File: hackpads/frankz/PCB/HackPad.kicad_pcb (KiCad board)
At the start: 2 copper layers, 63 x 82 mm, 29 parts, among them SW1 SW_Push_45deg, SW10 SW_Push_45deg, SW11 RotaryEncoder_Switch, SW12 RotaryEncoder_Switch, SW2 SW_Push_45deg, SW3 SW_Push_45deg, SW4 SW_Push_45deg, SW5 SW_Push_45deg, SW6 SW_Push_45deg, SW7 SW_Push_45deg, SW8 SW_Push_45deg, SW9 SW_Push_45deg, U2 MOUDLE-SEEEDUINO-XIAO

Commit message: Update PCB
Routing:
- net 1pinA: track 25.8 -> 24.6 mm
- net 1pinB: track 45.4 -> 44.6 mm
- net 2pinS2: track 110.3 -> 109.4 mm
- net 2pinB: track 70.9 -> 70.1 mm
- net 2pinA: track 59.5 -> 58.9 mm
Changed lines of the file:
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@@
 		(tags "Diode DO-35_SOD27 series Axial Horizontal pin pitch 7.62mm  length 4mm diameter 2mm")
 		(property "Reference" "D11"
-			(at 3.81 2.12 360)
+			(at 3.81 2.12 0)
 			(layer "B.SilkS")
 			(hide yes)
@@
 		)
 		(property "Value" "D"
-			(at 3.81 -2.12 360)
+			(at 3.81 -2.12 0)
 			(layer "B.Fab")
 			(hide yes)
@@
 		(tags "Diode DO-35_SOD27 series Axial Horizontal pin pitch 7.62mm  length 4mm diameter 2mm")
 		(property "Reference" "D10"
-			(at 3.81 2.12 360)
+			(at 3.81 2.12 0)
 			(layer "B.SilkS")
 			(hide yes)
@@
 		)
 		(property "Value" "D"
-			(at 3.81 -2.12 360)
+			(at 3.81 -2.12 0)
 			(layer "B.Fab")
 			(hide yes)
@@
 	)
 	(segment
-		(start 68.5 51.25)
-		(end 68.5 41.25)
-		(width 0.2)
-		(layer "B.Cu")
-		(net 19)
-	)
-	(segment
-		(start 67.440001 58.960001)
-		(end 67.440001 52.309999)
-		(width 0.2)
-		(layer "B.Cu")
-		(net 19)
-	)
-	(segment
 		(start 68.69 79.21)
 		(end 68.69 89.694365)
@@
 	)
 	(segment
+		(start 69 41.25)
+		(end 79.5 41.25)
+		(width 0.2)
+		(layer "B.Cu")
+		(net 19)
+	)
+	(segment
 		(start 61.565 36.55)
 		(end 63.8 36.55)
@@
 	)
 	(segment
-		(start 68.69 60.21)
+		(start 67.5 78.02)
+		(end 68.69 79.21)
+		(width 0.2)
+		(layer "B.Cu")
+		(net 19)
+	)
+	(segment
+		(start 67.440001 52.309999)
 		(end 67.440001 58.960001)
 		(width 0.2)
@@
 	)
 	(segment
-		(start 63.8 36.55)
-		(end 68.5 41.25)
+		(start 67.440001 58.960001)
+		(end 68.69 60.21)
 		(width 0.2)
 		(layer "B.Cu")
@@
 	)
 	(segment
-		(start 67.5 78.02)
-		(end 68.69 79.21)
+		(start 67.5 71.884365)
+		(end 67.5 78.02)
 		(width 0.2)
 		(layer "B.Cu")
@@
 	)
 	(segment
-		(start 68.5 41.25)
-		(end 79.5 41.25)
+		(start 68.69 70.694365)
+		(end 67.5 71.884365)
 		(width 0.2)
 		(layer "B.Cu")
@@
 	)
 	(segment
-		(start 67.440001 52.309999)
+		(start 68.5 41.25)
 		(end 68.5 51.25)
 		(width 0.2)
@@
 	)
 	(segment
-		(start 67.5 71.884365)
-		(end 67.5 78.02)
+		(start 67.59 90.794365)
+		(end 67.59 97.11)
 		(width 0.2)
 		(layer "B.Cu")
@@
 	)
 	(segment
-		(start 68.69 70.694365)
-		(end 67.5 71.884365)
+		(start 68.5 51.25)
+		(end 67.440001 52.309999)
 		(width 0.2)
 		(layer "B.Cu")
@@
 	)
 	(segment
-		(start 67.59 90.794365)
-		(end 67.59 97.11)
+		(start 68.5 41.75)
+		(end 69 41.25)
+		(width 0.2)
+		(layer "B.Cu")
+		(net 19)
+	)
+	(segment
+		(start 63.8 36.55)
+		(end 68.5 41.25)
 		(width 0.2)
 		(layer "B.Cu")
@@
 	)
 	(segment
+		(start 99 55.25)
+		(end 100.5 53.75)
+		(width 0.2)
+		(layer "B.Cu")
+		(net 20)
+	)
+	(segment
 		(start 100.5 43.25)
 		(end 98.5 41.25)
@@
 	)
 	(segment
-		(start 100.5 55.25)
+		(start 100.5 53.75)
 		(end 100.5 43.25)
 		(width 0.2)
@@
 	)
 	(segment
-		(start 91.5 55.25)
-		(end 100.5 55.25)
+		(start 87.69 79.21)
+		(end 87.69 89.694365)
 		(width 0.2)
 		(layer "B.Cu")
@@
 	)
 	(segment
-		(start 87.69 79.21)
-		(end 87.69 89.694365)
+		(start 87.645 70.739365)
+		(end 86.59 71.794365)
 		(width 0.2)
 		(layer "B.Cu")
@@
 	)
 	(segment
-		(start 87.645 70.739365)
-		(end 86.59 71.794365)
+		(start 87.69 59.06)
+		(end 91.5 55.25)
 		(width 0.2)
 		(layer "B.Cu")
@@
 	)
 	(segment
-		(start 86.59 97.11)
-		(end 87.69 98.21)
+		(start 91.5 55.25)
+		(end 99 55.25)
 		(width 0.2)
 		(layer "B.Cu")
@@
 	)
 	(segment
-		(start 87.69 59.06)
-		(end 91.5 55.25)
+		(start 86.59 97.11)
+		(end 87.69 98.21)
 		(width 0.2)
 		(layer "B.Cu")
@@
 	)
 	(segment
-		(start 59 40.25)
+		(start 51.26 36.25)
+		(end 58 36.25)
+		(width 0.2)
+		(layer "F.Cu")
+		(net 23)
+	)
+	(segment
+		(start 60 40.25)
 		(end 64 40.25)
 		(width 0.2)
@@
 	)
 	(segment
+		(start 45.88 41.63)
+		(end 51.26 36.25)
+		(width 0.2)
+		(layer "F.Cu")
+		(net 23)
+	)
+	(segment
+		(start 59 39.25)
+		(end 60 40.25)
+		(width 0.2)
+		(layer "F.Cu")
+		(net 23)
+	)
+	(segment
 		(start 64 40.25)
 		(end 65 41.25)
@@
 	)
 	(segment
-		(start 51.26 36.25)
-		(end 59 36.25)
+		(start 58 36.25)
+		(end 59 37.25)
 		(width 0.2)
 		(layer "F.Cu")
@@
 	)
 	(segment
-		(start 45.88 41.63)
-		(end 51.26 36.25)
+		(start 59 37.25)
+		(end 59 39.25)
 		(width 0.2)
 		(layer "F.Cu")
@@
 	)
 	(segment
-		(start 59 36.25)
-		(end 59 40.25)
+		(start 45.88 44.17)
+		(end 48 46.29)
 		(width 0.2)
 		(layer "F.Cu")
-		(net 23)
+		(net 24)
 	)
 	(segment
 		(start 48 46.29)
-		(end 48 54.75)
+		(end 48 53.75)
 		(width 0.2)
 		(layer "F.Cu")
@@
 	)
 	(segment
-		(start 45.88 44.17)
-		(end 48 46.29)
+		(start 48 53.75)
+		(end 49 54.75)
 		(width 0.2)
 		(layer "F.Cu")
@@
 	)
 	(segment
-		(start 71 54.75)
-		(end 71 52.25)
+		(start 49 54.75)
+		(end 70.5 54.75)
 		(width 0.2)
 		(layer "F.Cu")
@@
 	)
 	(segment
-		(start 48 54.75)
-		(end 71 54.75)
+		(start 70.5 54.75)
+		(end 71 54.25)
 		(width 0.2)
 		(layer "F.Cu")
@@
 	)
 	(segment
+		(start 71 54.25)
+		(end 71 52.25)
+		(width 0.2)
+		(layer "F.Cu")
+		(net 24)
+	)
+	(segment
+		(start 85.3 39.95)
+		(end 77.2 31.85)
+		(width 0.2)
+		(layer "B.Cu")
+		(net 25)
+	)
+	(segment
 		(start 85.3 44.95)
 		(end 85.3 39.95)
@@
 	)
 	(segment
-		(start 43 46.85)
-		(end 45.4 49.25)
+		(start 44.334314 31.85)
+		(end 43 33.184314)
+		(width 0.2)
+		(layer "B.Cu")
+		(net 25)
+	)
+	(segment
+		(start 77.2 31.85)
+		(end 44.334314 31.85)
 		(width 0.2)
 		(layer "B.Cu")
@@
 	)
 	(segment
-		(start 43 31.85)
+		(start 43 33.184314)
 		(end 43 46.85)
 		(width 0.2)
@@
 	)
 	(segment
-		(start 85.3 39.95)
-		(end 77.2 31.85)
+		(start 43 46.85)
+		(end 45.4 49.25)
 		(width 0.2)
 		(layer "B.Cu")
@@
 	)
 	(segment
-		(start 77.2 31.85)
-		(end 43 31.85)
+		(start 44.5 32.25)
+		(end 43.5 33.25)
 		(width 0.2)
 		(layer "B.Cu")
-		(net 25)
+		(net 26)
 	)
 	(segment
-		(start 84 41.25)
-		(end 75 32.25)
+		(start 43.5 33.25)
+		(end 43.5 44.81)
 		(width 0.2)
 		(layer "B.Cu")
@@
 	)
 	(segment
-		(start 75 32.25)
-		(end 43.5 32.25)
+		(start 43.5 44.81)
+		(end 45.4 46.71)
 		(width 0.2)
 		(layer "B.Cu")
@@
 	)
 	(segment
-		(start 43.5 32.25)
-		(end 43.5 44.81)
+		(start 84 41.25)
+		(end 75 32.25)
 		(width 0.2)
 		(layer "B.Cu")
@@
 	)
 	(segment
-		(start 43.5 44.81)
-		(end 45.4 46.71)
+		(start 75 32.25)
+		(end 44.5 32.25)
 		(width 0.2)
 		(layer "B.Cu")
@@
 		(polygon
 			(pts
-				(xy 33 25.25) (xy 117.5 25.25) (xy 117.5 128.75) (xy 28.5 128.25)
+				(xy 112 25.75) (xy 32 25.25) (xy 31.5 125.25) (xy 124 124.75)
 			)
 		)

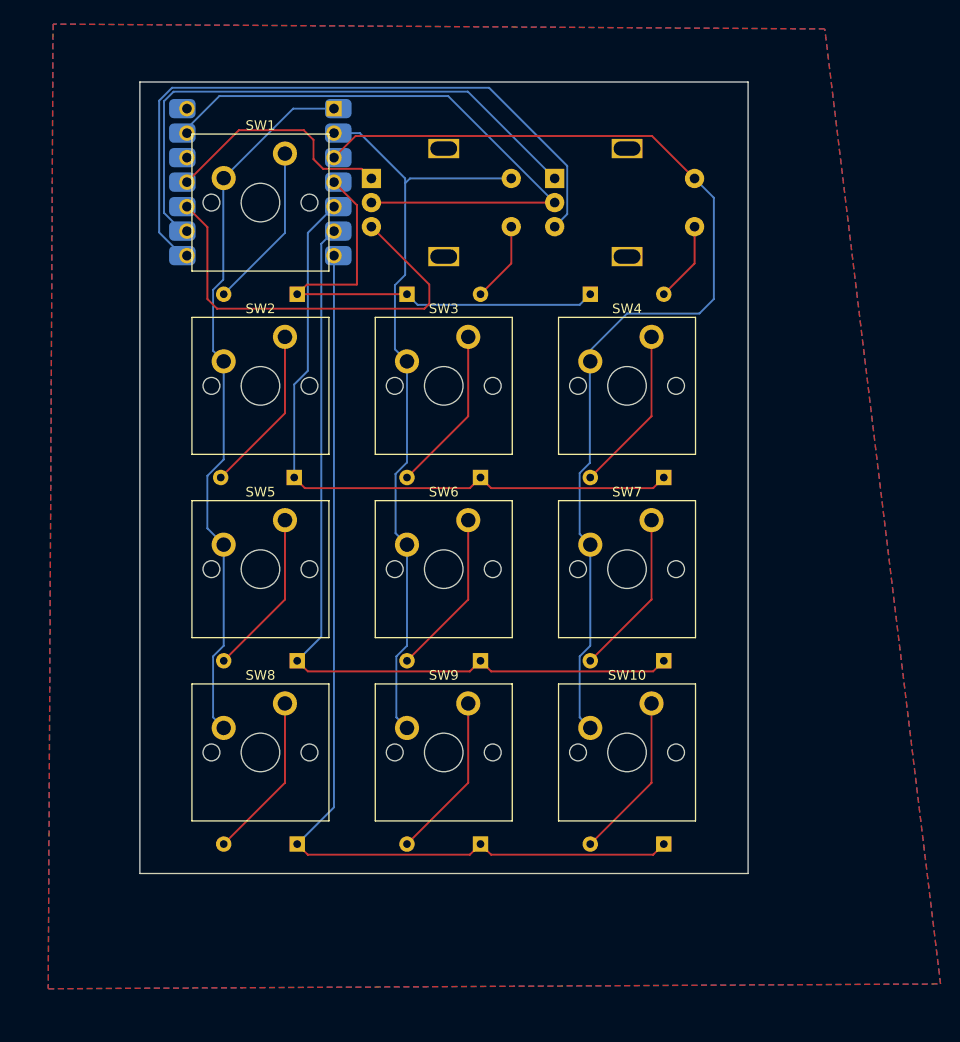
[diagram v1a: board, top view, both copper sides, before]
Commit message: Added production folder and reorganized
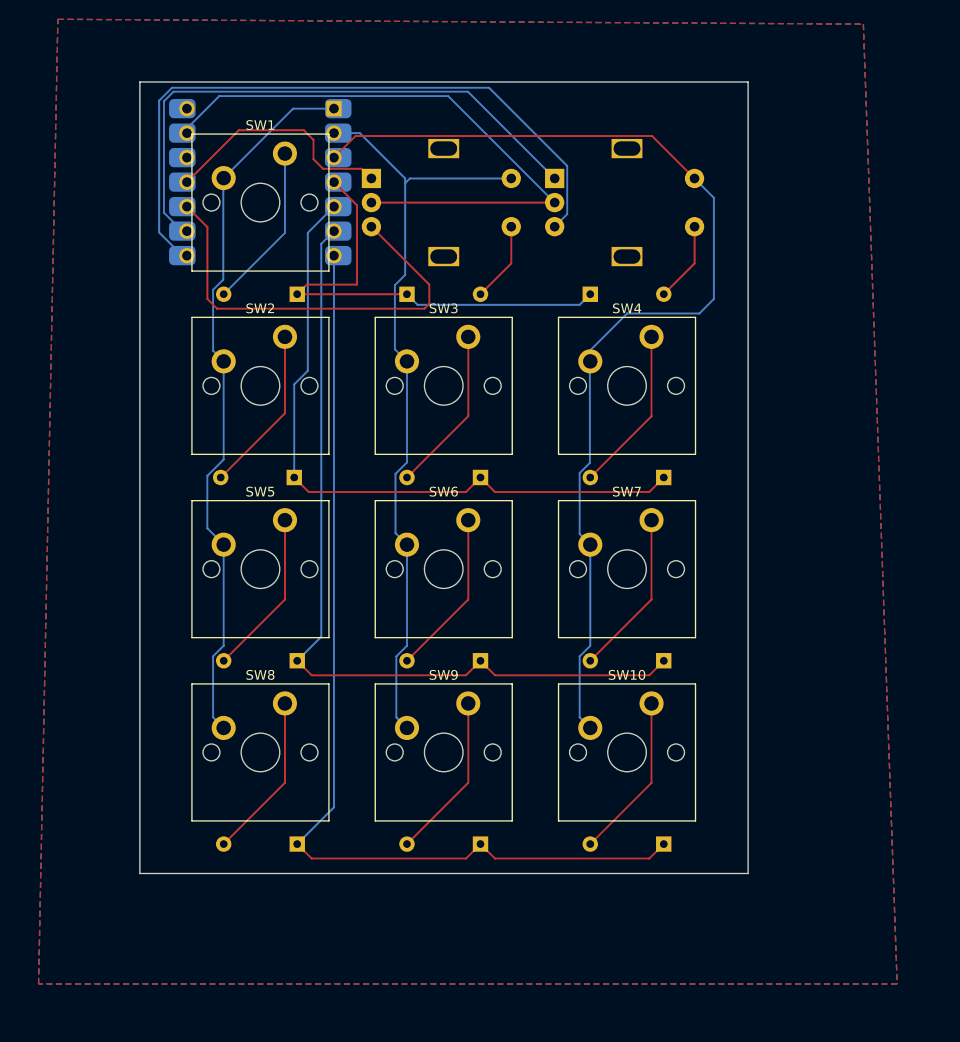
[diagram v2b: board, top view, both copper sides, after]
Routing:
- net ROW2: track 85.9 -> 86.6 mm
- net ROW3: track 102.4 -> 103.1 mm
- net ROW1: track 69.9 -> 70.6 mm
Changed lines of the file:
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@@
 			(usegerberattributes yes)
 			(usegerberadvancedattributes yes)
-			(creategerberjobfile yes)
+			(creategerberjobfile no)
 			(dashed_line_dash_ratio 12.000000)
 			(dashed_line_gap_ratio 3.000000)
@@
 			(psa4output no)
 			(plotreference yes)
-			(plotvalue yes)
+			(plotvalue no)
 			(plotfptext yes)
 			(plotinvisibletext no)
 			(sketchpadsonfab no)
-			(subtractmaskfromsilk no)
+			(subtractmaskfromsilk yes)
 			(outputformat 1)
 			(mirror no)
-			(drillshape 1)
+			(drillshape 0)
 			(scaleselection 1)
-			(outputdirectory "")
+			(outputdirectory "./")
 		)
 	)
@@
 	)
 	(segment
-		(start 58.1 73.35)
-		(end 75.21 73.35)
+		(start 77.81 73.75)
+		(end 93.81 73.75)
 		(width 0.2)
 		(layer "F.Cu")
@@
 	)
 	(segment
-		(start 94.21 73.35)
-		(end 95.31 72.25)
+		(start 74.81 73.75)
+		(end 76.31 72.25)
 		(width 0.2)
 		(layer "F.Cu")
@@
 	)
 	(segment
-		(start 75.21 73.35)
-		(end 76.31 72.25)
+		(start 93.81 73.75)
+		(end 95.31 72.25)
 		(width 0.2)
 		(layer "F.Cu")
@@
 	)
 	(segment
-		(start 77.41 73.35)
-		(end 94.21 73.35)
+		(start 76.31 72.25)
+		(end 77.81 73.75)
 		(width 0.2)
 		(layer "F.Cu")
@@
 	(segment
 		(start 57 72.25)
-		(end 58.1 73.35)
+		(end 58.5 73.75)
 		(width 0.2)
 		(layer "F.Cu")
@@
 	)
 	(segment
-		(start 76.31 72.25)
-		(end 77.41 73.35)
+		(start 58.5 73.75)
+		(end 74.81 73.75)
 		(width 0.2)
 		(layer "F.Cu")
@@
 	)
 	(segment
-		(start 75.21 92.35)
-		(end 76.31 91.25)
+		(start 58.81 92.75)
+		(end 74.81 92.75)
 		(width 0.2)
 		(layer "F.Cu")
@@
 	)
 	(segment
-		(start 57.31 91.25)
-		(end 58.41 92.35)
+		(start 74.81 92.75)
+		(end 76.31 91.25)
 		(width 0.2)
 		(layer "F.Cu")
@@
 	)
 	(segment
-		(start 76.31 91.25)
-		(end 77.41 92.35)
+		(start 77.81 92.75)
+		(end 93.81 92.75)
 		(width 0.2)
 		(layer "F.Cu")
@@
 	)
 	(segment
-		(start 58.41 92.35)
-		(end 75.21 92.35)
+		(start 93.81 92.75)
+		(end 95.31 91.25)
 		(width 0.2)
 		(layer "F.Cu")
@@
 	)
 	(segment
-		(start 94.21 92.35)
-		(end 95.31 91.25)
+		(start 76.31 91.25)
+		(end 77.81 92.75)
 		(width 0.2)
 		(layer "F.Cu")
@@
 	)
 	(segment
-		(start 77.41 92.35)
-		(end 94.21 92.35)
+		(start 57.31 91.25)
+		(end 58.81 92.75)
 		(width 0.2)
 		(layer "F.Cu")
@@
 	)
 	(segment
-		(start 77.41 111.35)
-		(end 94.21 111.35)
+		(start 76.31 110.25)
+		(end 77.81 111.75)
 		(width 0.2)
 		(layer "F.Cu")
@@
 	)
 	(segment
-		(start 76.31 110.25)
-		(end 77.41 111.35)
+		(start 93.81 111.75)
+		(end 95.31 110.25)
 		(width 0.2)
 		(layer "F.Cu")
@@
 	)
 	(segment
-		(start 57.31 110.25)
-		(end 58.41 111.35)
+		(start 74.81 111.75)
+		(end 76.31 110.25)
 		(width 0.2)
 		(layer "F.Cu")
@@
 	)
 	(segment
-		(start 58.41 111.35)
-		(end 75.21 111.35)
+		(start 57.31 110.25)
+		(end 58.81 111.75)
 		(width 0.2)
 		(layer "F.Cu")
@@
 	)
 	(segment
-		(start 75.21 111.35)
-		(end 76.31 110.25)
+		(start 58.81 111.75)
+		(end 74.81 111.75)
 		(width 0.2)
 		(layer "F.Cu")
@@
 	)
 	(segment
-		(start 94.21 111.35)
-		(end 95.31 110.25)
+		(start 77.81 111.75)
+		(end 93.81 111.75)
 		(width 0.2)
 		(layer "F.Cu")
@@
 		(polygon
 			(pts
-				(xy 112 25.75) (xy 32 25.25) (xy 31.5 125.25) (xy 124 124.75)
+				(xy 32.5 24.75) (xy 116 25.25) (xy 119.5 124.75) (xy 30.5 124.75)
 			)
 		)
